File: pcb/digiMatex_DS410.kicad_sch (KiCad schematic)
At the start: 51 parts, among them J1 POWER, J2 JTAG, J3 PROG, J4 Buttons, J5 SCALE, Q1 MMBT3904, Q2 MMBT3904, Q3 MMBT3904, SW1 SW_Push, SW2 SW_Push, U1 MAX7219, U2 L7805CDT-TR, U3 ESP32-WROOM-32E, U4 NCP1117DT33G

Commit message: use resistor footprints
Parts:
- R1, R10, R2, R4, R5, R8, R9: footprint Capacitor_SMD:C_0603_1608Metric -> Resistor_SMD:R_0603_1608Metric_Pad0.98x0.95mm_HandSolder
- R11, R12, R13: footprint Capacitor_SMD:C_0805_2012Metric -> Resistor_SMD:R_0805_2012Metric_Pad1.20x1.40mm_HandSolder
- R3, R6, R7: footprint Capacitor_SMD:C_0805_2012Metric -> Resistor_THT:R_Axial_DIN0207_L6.3mm_D2.5mm_P10.16mm_Horizontal
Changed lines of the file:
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@@
     (comment 1 "PCB to be maufactured by prototype board house (JLCPCB)")
   )
-  (bus_alias "Buttons" (members "b_display" "b_tare" "b_unit"))
-  (bus_alias "HX711" (members "SCK" "DT"))
-  (bus_alias "MAX7219" (members "CLK" "MOSI" "CS"))
-  (bus_alias "LED" (members "WiFi_LED" "lbs_LED" "kg_LED"))
   (bus_alias "7Seg" (members "A" "B" "C" "D" "E" "F" "G" "DP" "1" "2" "3" "4" "5" "6" "7" "0"))
+  (bus_alias "LED" (members "WiFi_LED" "lbs_LED" "kg_LED"))
+  (bus_alias "MAX7219" (members "CLK" "MOSI" "CS"))
+  (bus_alias "HX711" (members "SCK" "DT"))
+  (bus_alias "Buttons" (members "b_display" "b_tare" "b_unit"))
   (junction (at 110.49 34.29) (diameter 0) (color 0 0 0 0)
   )
@@
     (property "Reference" "R1" (id 0) (at 167.132 30.48 90))
     (property "Value" "10k" (id 1) (at 165.1 30.48 90))
-    (property "Footprint" "Capacitor_SMD:C_0603_1608Metric" (id 2) (at 163.322 30.48 90)
+    (property "Footprint" "Resistor_SMD:R_0603_1608Metric_Pad0.98x0.95mm_HandSolder" (id 2) (at 163.322 30.48 90)
       (effects (font (size 1.27 1.27)) hide)
     )
@@
     (property "Reference" "R7" (id 0) (at 128.27 111.252 90))
     (property "Value" "470" (id 1) (at 128.27 109.22 90))
-    (property "Footprint" "Capacitor_SMD:C_0805_2012Metric" (id 2) (at 128.27 107.442 90)
+    (property "Footprint" "Resistor_THT:R_Axial_DIN0207_L6.3mm_D2.5mm_P10.16mm_Horizontal" (id 2) (at 128.27 107.442 90)
       (effects (font (size 1.27 1.27)) hide)
     )
@@
     (property "Reference" "R9" (id 0) (at 47.752 170.18 90))
     (property "Value" "4k7" (id 1) (at 45.72 170.18 90))
-    (property "Footprint" "Capacitor_SMD:C_0603_1608Metric" (id 2) (at 43.942 170.18 90)
+    (property "Footprint" "Resistor_SMD:R_0603_1608Metric_Pad0.98x0.95mm_HandSolder" (id 2) (at 43.942 170.18 90)
       (effects (font (size 1.27 1.27)) hide)
     )
@@
     (property "Reference" "R5" (id 0) (at 119.38 118.872 90))
     (property "Value" "4k7" (id 1) (at 119.38 116.84 90))
-    (property "Footprint" "Capacitor_SMD:C_0603_1608Metric" (id 2) (at 119.38 115.062 90)
+    (property "Footprint" "Resistor_SMD:R_0603_1608Metric_Pad0.98x0.95mm_HandSolder" (id 2) (at 119.38 115.062 90)
       (effects (font (size 1.27 1.27)) hide)
     )
@@
     (property "Reference" "R11" (id 0) (at 91.44 145.288 90))
     (property "Value" "0" (id 1) (at 91.44 147.32 90))
-    (property "Footprint" "Capacitor_SMD:C_0805_2012Metric" (id 2) (at 91.44 149.098 90)
+    (property "Footprint" "Resistor_SMD:R_0805_2012Metric_Pad1.20x1.40mm_HandSolder" (id 2) (at 91.44 149.098 90)
       (effects (font (size 1.27 1.27)) hide)
     )
@@
     (property "Reference" "R2" (id 0) (at 119.38 98.552 90))
     (property "Value" "4k7" (id 1) (at 119.38 96.52 90))
-    (property "Footprint" "Capacitor_SMD:C_0603_1608Metric" (id 2) (at 119.38 94.742 90)
+    (property "Footprint" "Resistor_SMD:R_0603_1608Metric_Pad0.98x0.95mm_HandSolder" (id 2) (at 119.38 94.742 90)
       (effects (font (size 1.27 1.27)) hide)
     )
@@
     (property "Reference" "R12" (id 0) (at 91.44 150.368 90))
     (property "Value" "0" (id 1) (at 91.44 152.4 90))
-    (property "Footprint" "Capacitor_SMD:C_0805_2012Metric" (id 2) (at 91.44 154.178 90)
+    (property "Footprint" "Resistor_SMD:R_0805_2012Metric_Pad1.20x1.40mm_HandSolder" (id 2) (at 91.44 154.178 90)
       (effects (font (size 1.27 1.27)) hide)
     )
@@
     (property "Reference" "R10" (id 0) (at 71.882 180.34 90))
     (property "Value" "4k7" (id 1) (at 69.85 180.34 90))
-    (property "Footprint" "Capacitor_SMD:C_0603_1608Metric" (id 2) (at 68.072 180.34 90)
+    (property "Footprint" "Resistor_SMD:R_0603_1608Metric_Pad0.98x0.95mm_HandSolder" (id 2) (at 68.072 180.34 90)
       (effects (font (size 1.27 1.27)) hide)
     )
@@
     (property "Reference" "R4" (id 0) (at 119.38 78.232 90))
     (property "Value" "4k7" (id 1) (at 119.38 76.2 90))
-    (property "Footprint" "Capacitor_SMD:C_0603_1608Metric" (id 2) (at 119.38 74.422 90)
+    (property "Footprint" "Resistor_SMD:R_0603_1608Metric_Pad0.98x0.95mm_HandSolder" (id 2) (at 119.38 74.422 90)
       (effects (font (size 1.27 1.27)) hide)
     )
@@
     (property "Reference" "R3" (id 0) (at 128.27 90.932 90))
     (property "Value" "470" (id 1) (at 128.27 88.9 90))
-    (property "Footprint" "Capacitor_SMD:C_0805_2012Metric" (id 2) (at 128.27 87.122 90)
+    (property "Footprint" "Resistor_THT:R_Axial_DIN0207_L6.3mm_D2.5mm_P10.16mm_Horizontal" (id 2) (at 128.27 87.122 90)
       (effects (font (size 1.27 1.27)) hide)
     )
@@
     (property "Reference" "R6" (id 0) (at 128.27 70.612 90))
     (property "Value" "470" (id 1) (at 128.27 68.58 90))
-    (property "Footprint" "Capacitor_SMD:C_0805_2012Metric" (id 2) (at 128.27 66.802 90)
+    (property "Footprint" "Resistor_THT:R_Axial_DIN0207_L6.3mm_D2.5mm_P10.16mm_Horizontal" (id 2) (at 128.27 66.802 90)
       (effects (font (size 1.27 1.27)) hide)
     )
@@
     (property "Reference" "R8" (id 0) (at 23.622 170.18 90))
     (property "Value" "10k" (id 1) (at 21.59 170.18 90))
-    (property "Footprint" "Capacitor_SMD:C_0603_1608Metric" (id 2) (at 19.812 170.18 90)
+    (property "Footprint" "Resistor_SMD:R_0603_1608Metric_Pad0.98x0.95mm_HandSolder" (id 2) (at 19.812 170.18 90)
       (effects (font (size 1.27 1.27)) hide)
     )
@@
     (property "Reference" "R13" (id 0) (at 119.38 144.018 90))
     (property "Value" "0" (id 1) (at 119.38 146.05 90))
-    (property "Footprint" "Capacitor_SMD:C_0805_2012Metric" (id 2) (at 119.38 147.828 90)
+    (property "Footprint" "Resistor_SMD:R_0805_2012Metric_Pad1.20x1.40mm_HandSolder" (id 2) (at 119.38 147.828 90)
       (effects (font (size 1.27 1.27)) hide)
     )
@@
     )
     (path "/251fb91c-a24a-491a-b294-4062bba2b097"
-      (reference "R1") (unit 1) (value "10k") (footprint "Capacitor_SMD:C_0603_1608Metric")
+      (reference "R1") (unit 1) (value "10k") (footprint "Resistor_SMD:R_0603_1608Metric_Pad0.98x0.95mm_HandSolder")
     )
     (path "/76f45159-d670-4a54-ac6e-4cff51276cad"
-      (reference "R2") (unit 1) (value "4k7") (footprint "Capacitor_SMD:C_0603_1608Metric")
+      (reference "R2") (unit 1) (value "4k7") (footprint "Resistor_SMD:R_0603_1608Metric_Pad0.98x0.95mm_HandSolder")
     )
     (path "/c2d2960b-5f4a-4e77-9c2d-aaad7da1b1dd"
-      (reference "R3") (unit 1) (value "470") (footprint "Capacitor_SMD:C_0805_2012Metric")
+      (reference "R3") (unit 1) (value "470") (footprint "Resistor_THT:R_Axial_DIN0207_L6.3mm_D2.5mm_P10.16mm_Horizontal")
     )
     (path "/b3331c42-7727-4715-8a34-175370d6f718"
-      (reference "R4") (unit 1) (value "4k7") (footprint "Capacitor_SMD:C_0603_1608Metric")
+      (reference "R4") (unit 1) (value "4k7") (footprint "Resistor_SMD:R_0603_1608Metric_Pad0.98x0.95mm_HandSolder")
     )
     (path "/6eb23b4a-8597-43d2-90da-071bec110e67"
-      (reference "R5") (unit 1) (value "4k7") (footprint "Capacitor_SMD:C_0603_1608Metric")
+      (reference "R5") (unit 1) (value "4k7") (footprint "Resistor_SMD:R_0603_1608Metric_Pad0.98x0.95mm_HandSolder")
     )
     (path "/cf5cee02-f0d1-4533-9202-c9e1e8e2219d"
-      (reference "R6") (unit 1) (value "470") (footprint "Capacitor_SMD:C_0805_2012Metric")
+      (reference "R6") (unit 1) (value "470") (footprint "Resistor_THT:R_Axial_DIN0207_L6.3mm_D2.5mm_P10.16mm_Horizontal")
     )
     (path "/26ce88ea-8a7b-491e-a098-0c2864b95850"
-      (reference "R7") (unit 1) (value "470") (footprint "Capacitor_SMD:C_0805_2012Metric")
+      (reference "R7") (unit 1) (value "470") (footprint "Resistor_THT:R_Axial_DIN0207_L6.3mm_D2.5mm_P10.16mm_Horizontal")
     )
     (path "/d2c92adf-1fe1-47c3-8ff6-f267b017628c"
-      (reference "R8") (unit 1) (value "10k") (footprint "Capacitor_SMD:C_0603_1608Metric")
+      (reference "R8") (unit 1) (value "10k") (footprint "Resistor_SMD:R_0603_1608Metric_Pad0.98x0.95mm_HandSolder")
     )
     (path "/37838864-ef06-4e83-a4fe-ae38d5de2860"
-      (reference "R9") (unit 1) (value "4k7") (footprint "Capacitor_SMD:C_0603_1608Metric")
+      (reference "R9") (unit 1) (value "4k7") (footprint "Resistor_SMD:R_0603_1608Metric_Pad0.98x0.95mm_HandSolder")
     )
     (path "/9af31413-ac38-4a46-b544-a0d1966a9c82"
-      (reference "R10") (unit 1) (value "4k7") (footprint "Capacitor_SMD:C_0603_1608Metric")
+      (reference "R10") (unit 1) (value "4k7") (footprint "Resistor_SMD:R_0603_1608Metric_Pad0.98x0.95mm_HandSolder")
     )
     (path "/76ebd3fa-fd01-48cb-a974-a7709d15fef3"
-      (reference "R11") (unit 1) (value "0") (footprint "Capacitor_SMD:C_0805_2012Metric")
+      (reference "R11") (unit 1) (value "0") (footprint "Resistor_SMD:R_0805_2012Metric_Pad1.20x1.40mm_HandSolder")
     )
     (path "/94f916f9-7860-46b4-b120-80b49efd90d9"
-      (reference "R12") (unit 1) (value "0") (footprint "Capacitor_SMD:C_0805_2012Metric")
+      (reference "R12") (unit 1) (value "0") (footprint "Resistor_SMD:R_0805_2012Metric_Pad1.20x1.40mm_HandSolder")
     )
     (path "/fe8ba7db-3f8f-451d-9a2f-2963aabd7f90"
-      (reference "R13") (unit 1) (value "0") (footprint "Capacitor_SMD:C_0805_2012Metric")
+      (reference "R13") (unit 1) (value "0") (footprint "Resistor_SMD:R_0805_2012Metric_Pad1.20x1.40mm_HandSolder")
     )
     (path "/309f9ac3-284d-4459-9769-17ef709da47c"

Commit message: rev A layout
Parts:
- removed HS1: Heatsink, pl_heatsink:TO-220hs_16x16x25mm_2pins, symbol Mechanical:Heatsink
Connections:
- net b_display: now also U3.31 (IO19); no longer U3.33 (IO21)
- net b_unit: now also U3.33 (IO21); no longer U3.31 (IO19)
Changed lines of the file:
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@@
-    (stroke (width 0) (type default) (color 0 0 0 0))
-  )
-  (polyline (pts (xy 85.09 25.4) (xy 85.09 26.67))
     (stroke (width 0) (type default) (color 0 0 0 0))
   )
@@
     (stroke (width 0) (type default) (color 0 0 0 0))
   )
-  (polyline (pts (xy 85.09 26.67) (xy 85.09 31.75))
-    (stroke (width 0) (type default) (color 0 0 0 0))
-  )
   (polyline (pts (xy 204.47 163.83) (xy 154.94 163.83))
     (stroke (width 0) (type default) (color 0 0 0 0))
@@
     (effects (font (size 1.27 1.27)) (justify left bottom))
   )
-  (label "b_unit" (at 64.77 114.3 0)
+  (label "b_unit" (at 64.77 116.84 0)
     (effects (font (size 1.27 1.27)) (justify left bottom))
   )
@@
     (effects (font (size 1.27 1.27)) (justify left bottom))
   )
-  (label "b_display" (at 64.77 116.84 0)
+  (label "b_display" (at 64.77 114.3 0)
     (effects (font (size 1.27 1.27)) (justify left bottom))
   )
@@
     (pin "1")
   )
-  (symbol (lib_id "Mechanical:Heatsink") (at 85.09 25.4 0) (unit 1)
-    (in_bom yes) (on_board yes)
-    (property "Reference" "HS1" (id 0) (at 85.09 20.32 0))
-    (property "Value" "Heatsink" (id 1) (at 85.09 26.67 0)
-      (effects (font (size 1.27 1.27)) hide)
-    )
-    (property "Footprint" "pl_heatsink:TO-220hs_16x16x25mm_2pins" (id 2) (at 85.3948 25.4 0)
-      (effects (font (size 1.27 1.27)) hide)
-    )
-    (property "Datasheet" "~" (id 3) (at 85.3948 25.4 0)
-      (effects (font (size 1.27 1.27)) hide)
-    )
-  )
   (symbol (lib_id "Device:R") (at 119.38 146.05 90) (unit 1)
     (in_bom yes) (on_board yes)
@@
       (reference "H4") (unit 1) (value "MountingHole") (footprint "MountingHole:MountingHole_4mm_Pad")
     )
-    (path "/fbb7b3f5-b61c-4411-a813-3930d80b07fc"
-      (reference "HS1") (unit 1) (value "Heatsink") (footprint "pl_heatsink:TO-220hs_16x16x25mm_2pins")
-    )
     (path "/34c53cff-c073-4b59-a48d-10c7e18a985b"

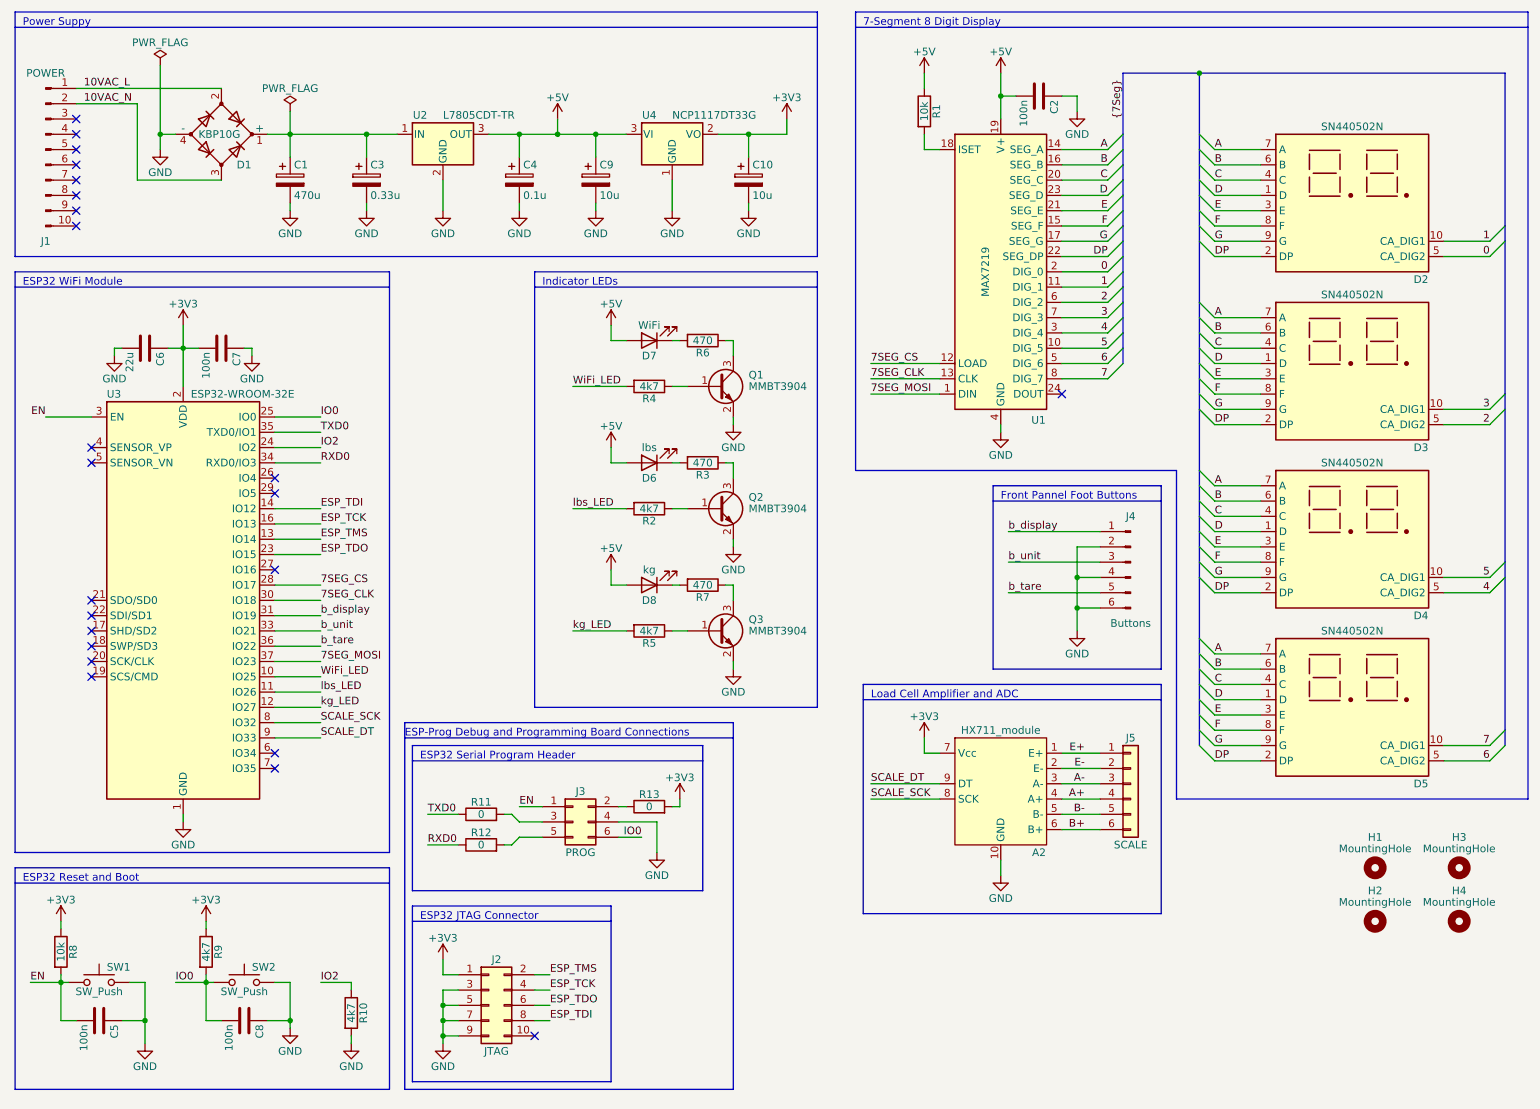
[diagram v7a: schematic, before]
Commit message: add HX711 IC to main board
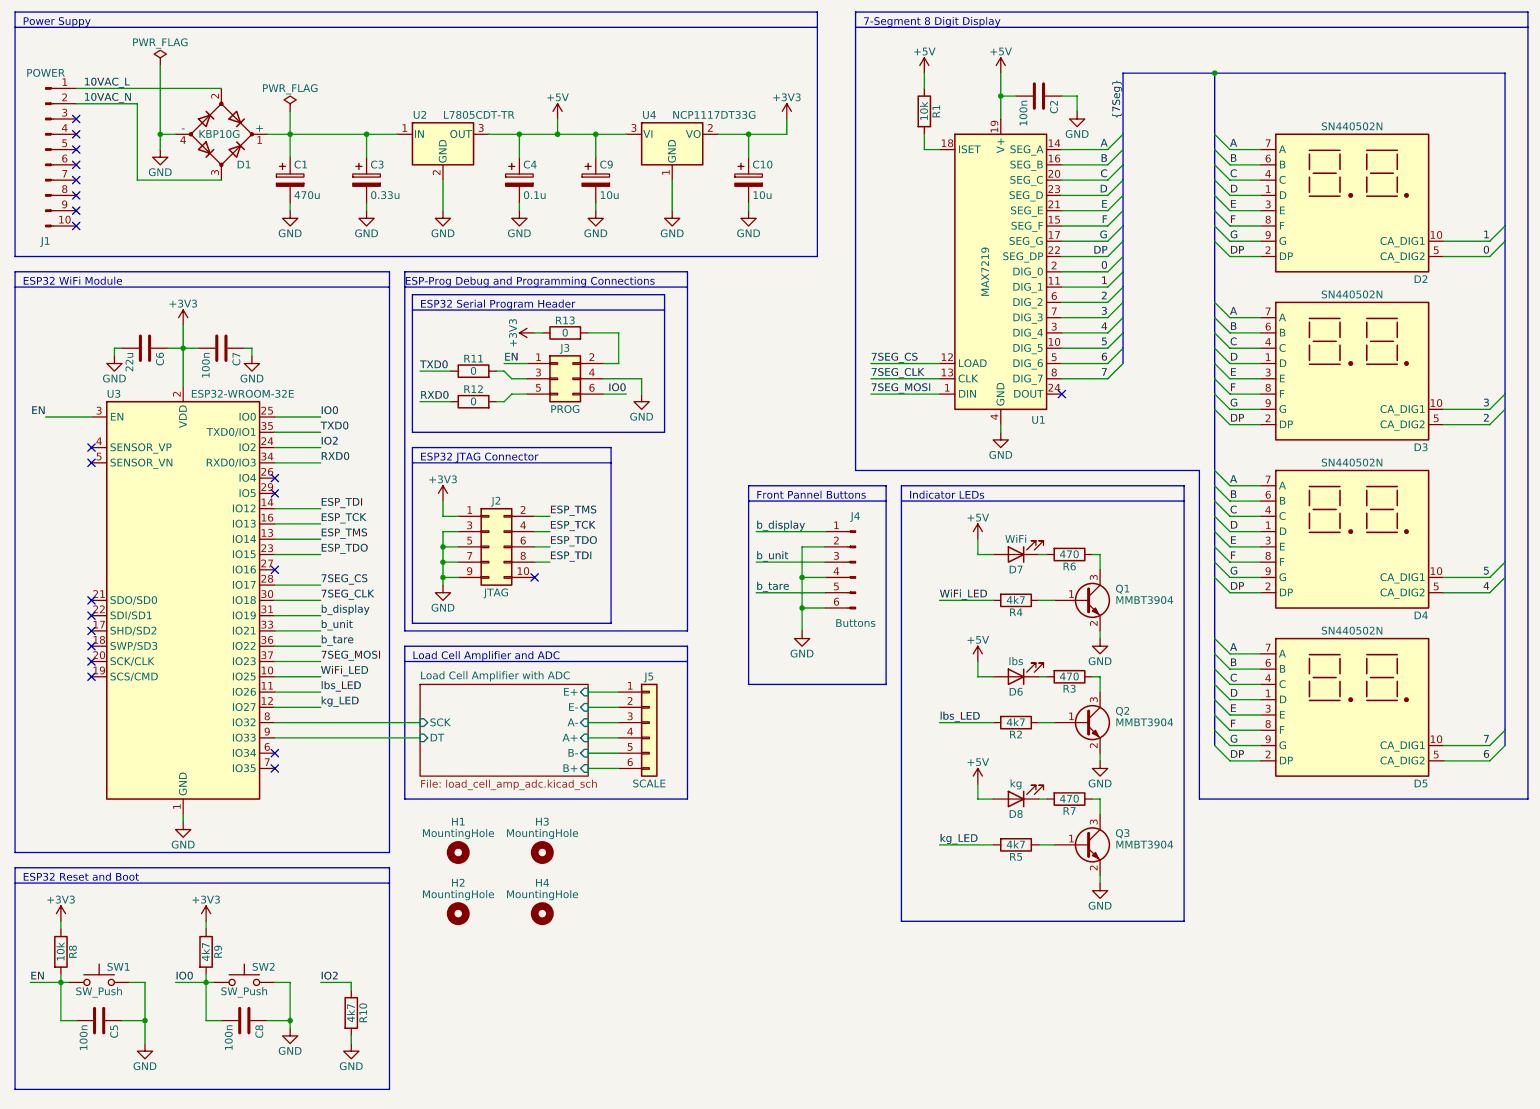
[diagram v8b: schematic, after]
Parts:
- removed A2: HX711_module, pl_scale:HX711_module, symbol pl_scale:HX711_module
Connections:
- net +3V3: now also R13.1; no longer R13.2
- net at J3.2 (Pin_2): now also R13.2; no longer R13.1
- net A+ renamed Load Cell Amplifier with ADC/A+
- net A- renamed Load Cell Amplifier with ADC/A-
- net B+ renamed Load Cell Amplifier with ADC/B+
- net B- renamed Load Cell Amplifier with ADC/B-
- net E+ renamed Load Cell Amplifier with ADC/E+
- net E- renamed Load Cell Amplifier with ADC/E-
- net SCALE_DT renamed Load Cell Amplifier with ADC/DT
- net SCALE_SCK renamed Load Cell Amplifier with ADC/SCK
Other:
- added sheet Load Cell Amplifier with ADC (load_cell_amp_adc.kicad_sch)
- note added: "ESP-Prog Debug and Programming Connections"
- note added: "Front Pannel Buttons"
- note removed: "ESP-Prog Debug and Programming Board Connections"
- note removed: "Front Pannel Foot Buttons"
- moved on the sheet: D6, D7, D8, H1, H2, H3, H4, J2, J3, J4, J5, Q1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
